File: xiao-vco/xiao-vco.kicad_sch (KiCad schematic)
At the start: 50 parts, among them J1 C2M, J2 C2F, J3 Eurorack Power, J4 CV1, J5 V/OCT, J6 OUT, J7 CV2, J8 C1M, J9 C1F, U1 SeeeduinoXIAO, U2 MCP6004, U3 LM4040DBZ-10, U4 TL072, U5 LM1117-5.0

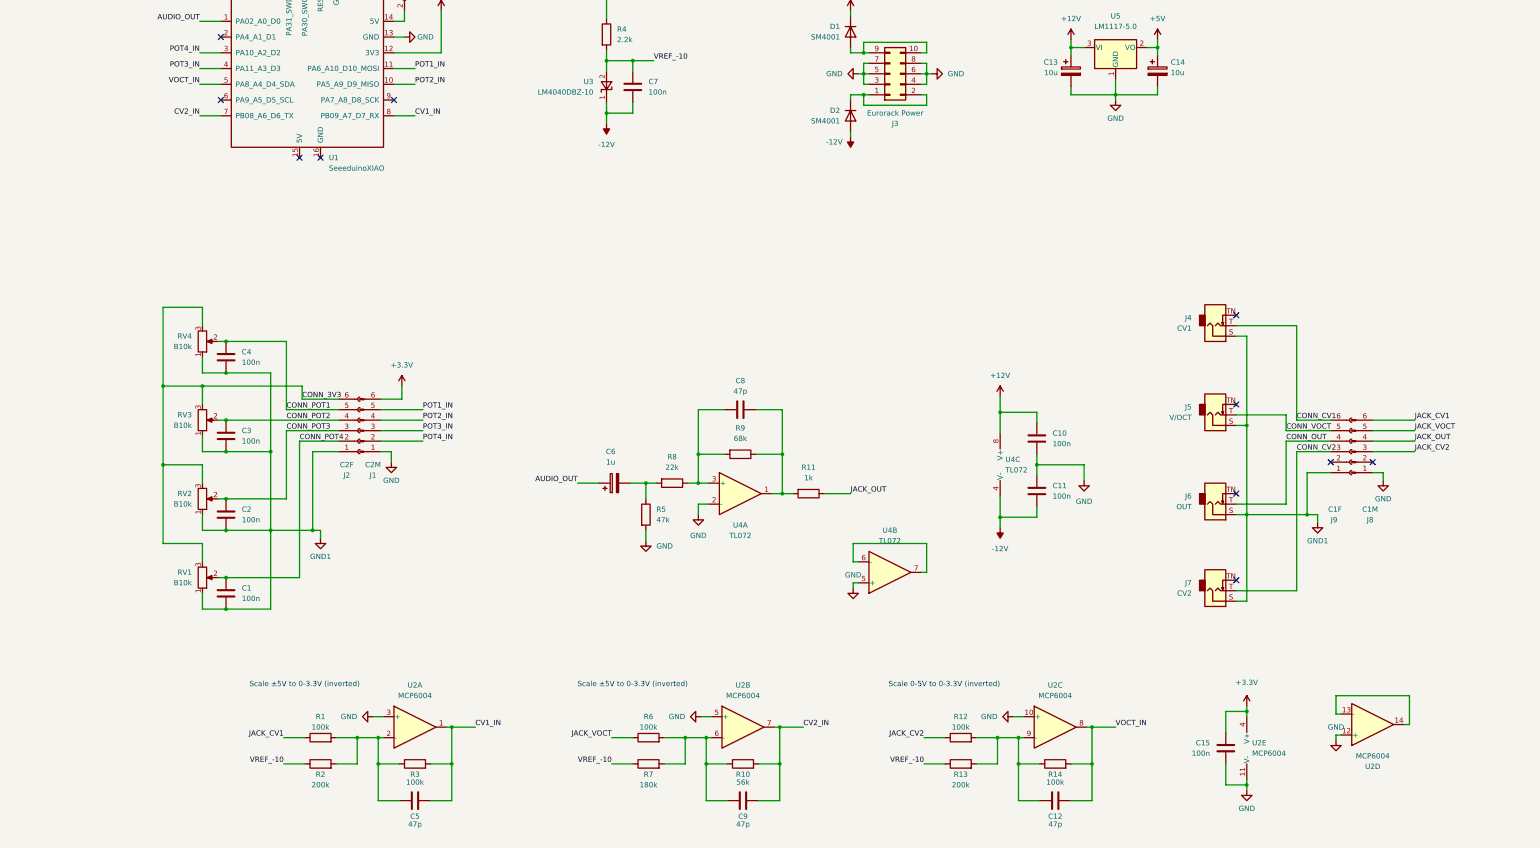
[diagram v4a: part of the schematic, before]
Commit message: Change MCP6004 to 6002 for availability
JLCPCB has MCP6002 in basic range.
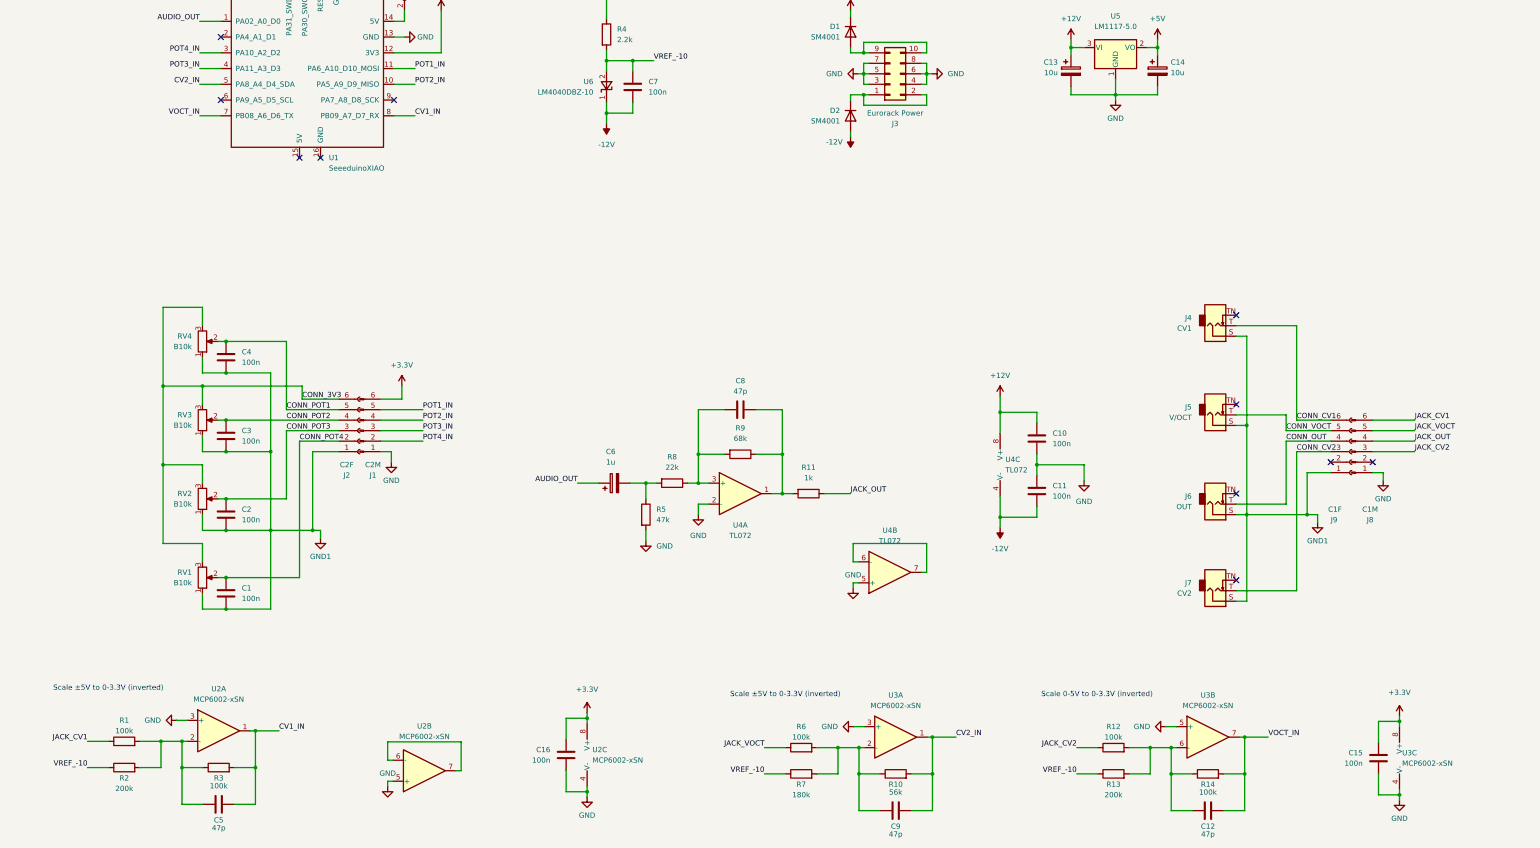
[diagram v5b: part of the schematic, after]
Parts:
- removed U2: MCP6004, Package_SO:SOIC-14_3.9x8.7mm_P1.27mm, symbol Amplifier_Operational:MCP6004
- added C16: 100n, Capacitor_SMD:C_0603_1608Metric_Pad1.08x0.95mm_HandSolder, symbol Device:C
- added U2, U3: MCP6002-xSN, Package_SO:SOIC-8_3.9x4.9mm_P1.27mm, symbol Amplifier_Operational:MCP6002-xSN
- U4: footprint Package_SO:SOIC-14_3.9x8.7mm_P1.27mm -> Package_SO:SOIC-8_3.9x4.9mm_P1.27mm
- renumbered U3 to U6
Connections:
- net +3V3: now also C16.1, U2.8 (V+), U3.8 (V+)
- net CV1_IN: now also U2.1
- net CV2_IN: now also U1.5 (PA8_A4_D4_SDA), U3.1; no longer U1.7 (PB08_A6_D6_TX)
- net GND: now also C16.2, U2.3 (+), U2.4 (V-), U2.5 (+), U3.3 (+), U3.4 (V-), U3.5 (+)
- net VOCT_IN: now also U1.7 (PB08_A6_D6_TX), U3.7; no longer U1.5 (PA8_A4_D4_SDA)
- net at C5.1, R1.2, R2.2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: now also U2.2 (-)
- net at C9.1, R10.1, R6.2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: now also U3.2 (-)
- net at C12.1, R12.2, R13.2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: now also U3.6 (-)
- new net: U2.6 (-), U2.7
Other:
- moved on the sheet: C12, C15, C5, C9, R1, R10, R12, R13, R14, R2, R3, R6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

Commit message: Add LED
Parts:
- added D3: LED, LED_THT:LED_D3.0mm, symbol Device:LED
- added R15: 68, Resistor_SMD:R_0603_1608Metric, symbol Device:R
- C1, C10, C11, C12, C15, C16, C2, C3, C4, C5, C7, C8, C9: footprint Capacitor_SMD:C_0603_1608Metric_Pad1.08x0.95mm_HandSolder -> Capacitor_SMD:C_0603_1608Metric
- J4, J5, J6, J7: footprint Connector_Audio:Jack_3.5mm_QingPu_WQP-PJ398SM_Vertical_CircularHoles -> Personal:Thonkiconn
- R1, R10, R11, R12, R13, R14, R2, R3, R4, R5, R6, R7, R8, R9: footprint Resistor_SMD:R_0603_1608Metric_Pad0.98x0.95mm_HandSolder -> Resistor_SMD:R_0603_1608Metric
- RV1: footprint Personal:Potentiometer_Alpha_RD901F-40-00D_Single_Vertical-Hanging -> Personal:Alpha_9mm_Pot_Overhanging
- RV2, RV3, RV4: footprint Potentiometer_THT:Potentiometer_Alpha_RD901F-40-00D_Single_Vertical -> Personal:Alpha_9mm_Pot
- U2: footprint (none) -> Package_SO:SOIC-8_3.9x4.9mm_P1.27mm
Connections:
- net GND1: now also R15.2
- net LED: now reaches J8.2 (Pin_2)
- net LED: now also U1.6 (PA9_A5_D5_SCL)
- net CONN_LED: now reaches J9.2 (Pin_2)
- net CONN_LED: now also D3.2 (A)
- new net: D3.1 (K), R15.1
- no-connect marks 15 -> 12

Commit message: Add switchable 5/8V output
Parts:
- removed C6: 1u, Capacitor_SMD:C_Elec_5x5.8, symbol Device:CP
- added C17: 47p, Capacitor_SMD:C_0603_1608Metric, symbol Device:C
- added C18, C19, C20: 1n, Capacitor_SMD:C_0603_1608Metric, symbol Device:C
- added C6: 1u, Capacitor_SMD:C_Elec_4x5.4, symbol Device:C_Polarized
- added JP2: Output range, Connector_PinHeader_2.54mm:PinHeader_1x02_P2.54mm_Vertical, symbol Jumper:Jumper_2_Bridged
- added R16, R21: 100k, Resistor_SMD:R_0603_1608Metric, symbol Device:R
- added R17: 330k, Resistor_SMD:R_0603_1608Metric, symbol Device:R
- added R18: 200k, Resistor_SMD:R_0603_1608Metric, symbol Device:R
- added R19: 13k, Resistor_SMD:R_0603_1608Metric, symbol Device:R
- added R20: 20k, Resistor_SMD:R_0603_1608Metric, symbol Device:R
- C1, C10, C11, C15, C16, C2, C3, C4, C7: LCSC C14663 -> (none)
- C12, C8, C9: LCSC C1671 -> (none)
- C13, C14: footprint Capacitor_SMD:C_Elec_5x5.8 -> Capacitor_SMD:C_Elec_4x5.4
- D1, D2: LCSC C64898 -> (none)
- R1, R12, R3, R6: LCSC C25803 -> (none)
- R10: value 56k -> 100k; LCSC C23206 -> (none)
- R11: LCSC C21190 -> (none)
- R13: value 200k -> 180k; LCSC C25811 -> (none)
- R14: value 100k -> 56k; LCSC C25803 -> (none)
- R2: LCSC C25811 -> (none)
- R4: LCSC C4190 -> (none)
- R5: value 47k -> 100k; LCSC C25819 -> (none)
- R7: value 180k -> 200k; LCSC C22827 -> (none)
- R8: value 22k -> 100k; LCSC C31850 -> (none)
- R9: value 68k -> 100k; LCSC C23231 -> (none)
- U4: LCSC C6961 -> (none)
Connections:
- net +3V3: now also R5.1, R17.1
- net AUDIO_OUT: now also R8.2
- net CONN_CV1: now also C19.1
- net CONN_CV2: now also C20.1
- net CONN_VOCT: now also C18.1
- net CV1_IN: now also C9.2, R10.2, U3.1; no longer C5.2, R3.2, U2.1
- net CV2_IN: now also C5.2, R3.2, U1.6 (PA9_A5_D5_SCL), U2.1; no longer C9.2, R10.2, U1.5 (PA8_A4_D4_SDA), U3.1
- net GND: now also U4.3 (+), C6.2, R16.2, R18.2; no longer R5.2, U2.5 (+), U4.2 (-), U4.5 (+)
- net GND1: now also C18.2, C19.2, C20.2
- net JACK_CV1: now also R6.1; no longer R1.1
- net JACK_CV2: now also R1.1; no longer R12.1
- net JACK_VOCT: now also R12.1; no longer R6.1
- net LED: now also U1.7 (PB08_A6_D6_TX); no longer U1.6 (PA9_A5_D5_SCL)
- net VOCT_IN: now also U1.5 (PA8_A4_D4_SDA); no longer U1.7 (PB08_A6_D6_TX)
- net at R11.2, U4.1: now also C17.1, R21.1; no longer C8.1, R9.1
- net at C8.2, R8.1, R9.2: now also U4.6 (-); no longer U4.3 (+)
- net at U4.7: now also C8.1, R9.1, JP2.1 (A), R19.2; no longer U4.6 (-)
- new net: C17.2, R20.1, R21.2, U4.2 (-)
- new net: JP2.2 (B), R19.1, R20.2
- new net: R16.1, R5.2, U2.5 (+)
- new net VBIAS: C6.1, R17.2, R18.1, U4.5 (+)
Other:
- moved on the sheet: C10, C11, C13, C14, C15, C5, C7, C8, C9, D1, D2, D3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

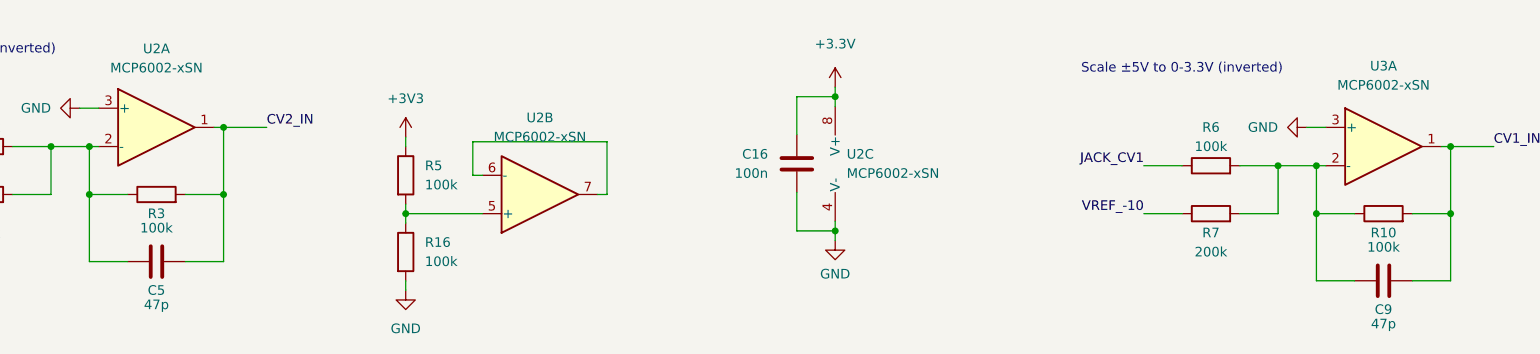
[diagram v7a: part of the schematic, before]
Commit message: Tweak layout, fix CV gain
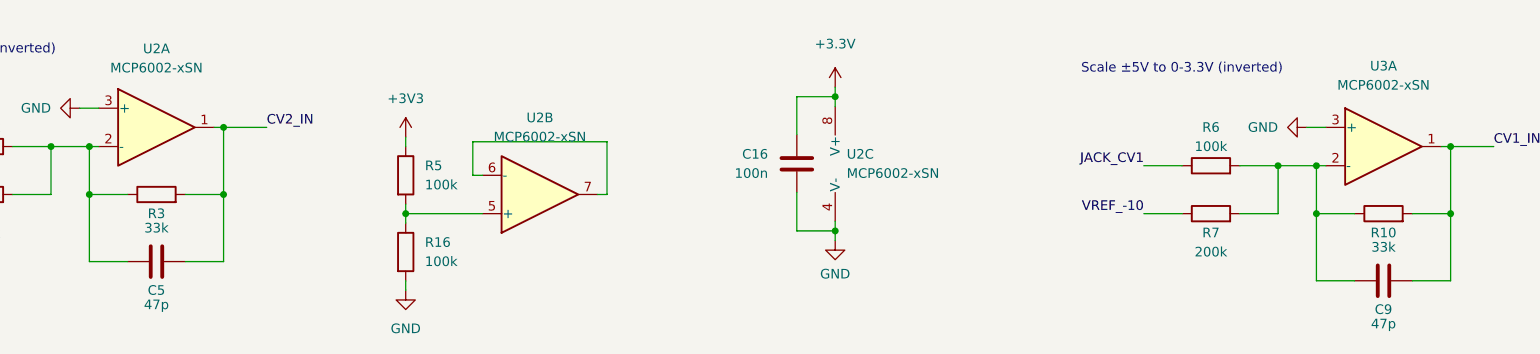
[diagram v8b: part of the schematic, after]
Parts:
- D1, D2: footprint Personal:SOD-123FL -> Diode_THT:D_DO-41_SOD81_P10.16mm_Horizontal
- R10, R3: value 100k -> 33k
